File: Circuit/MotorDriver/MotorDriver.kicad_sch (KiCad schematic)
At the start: 21 parts, among them J3 Conn_01x03_Pin, J4 Conn_01x04_Pin, J5 Conn_01x06_Pin, U3 DRV8316RRGFR, U4 XC6206PxxxMR

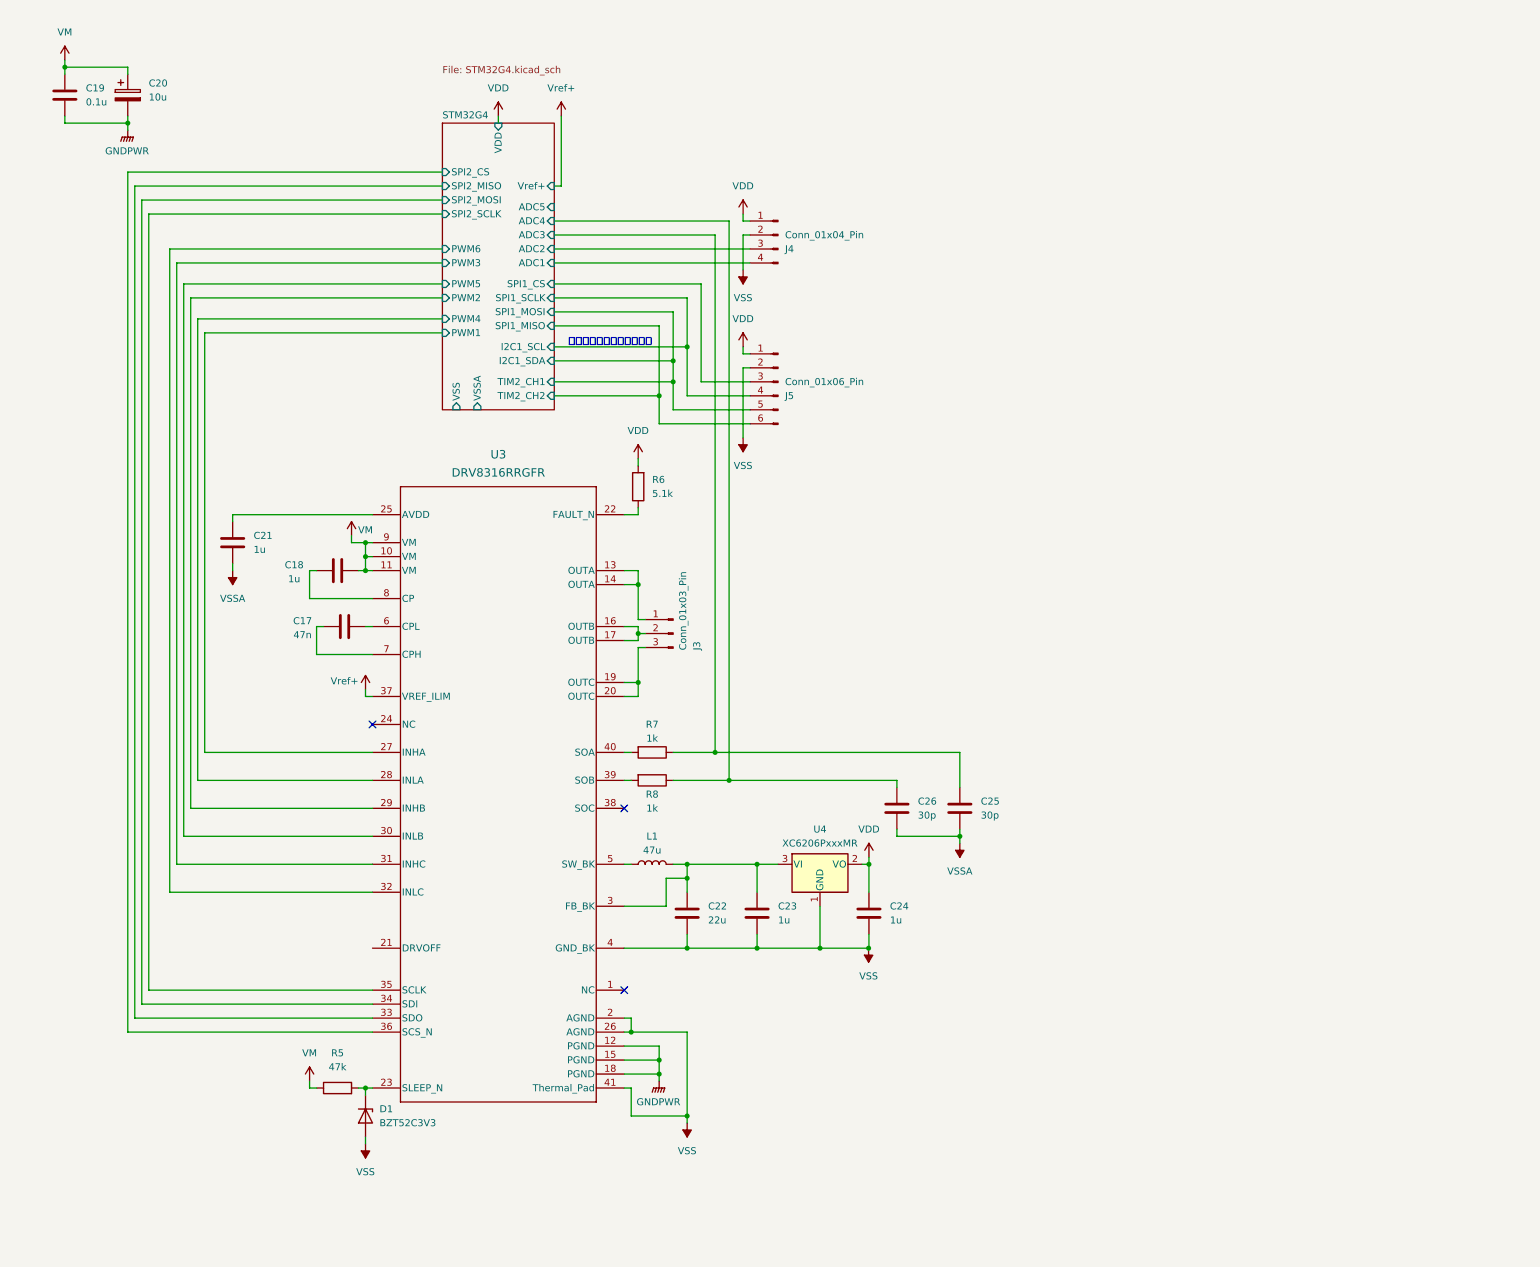
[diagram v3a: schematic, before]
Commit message: GPIOの配線等
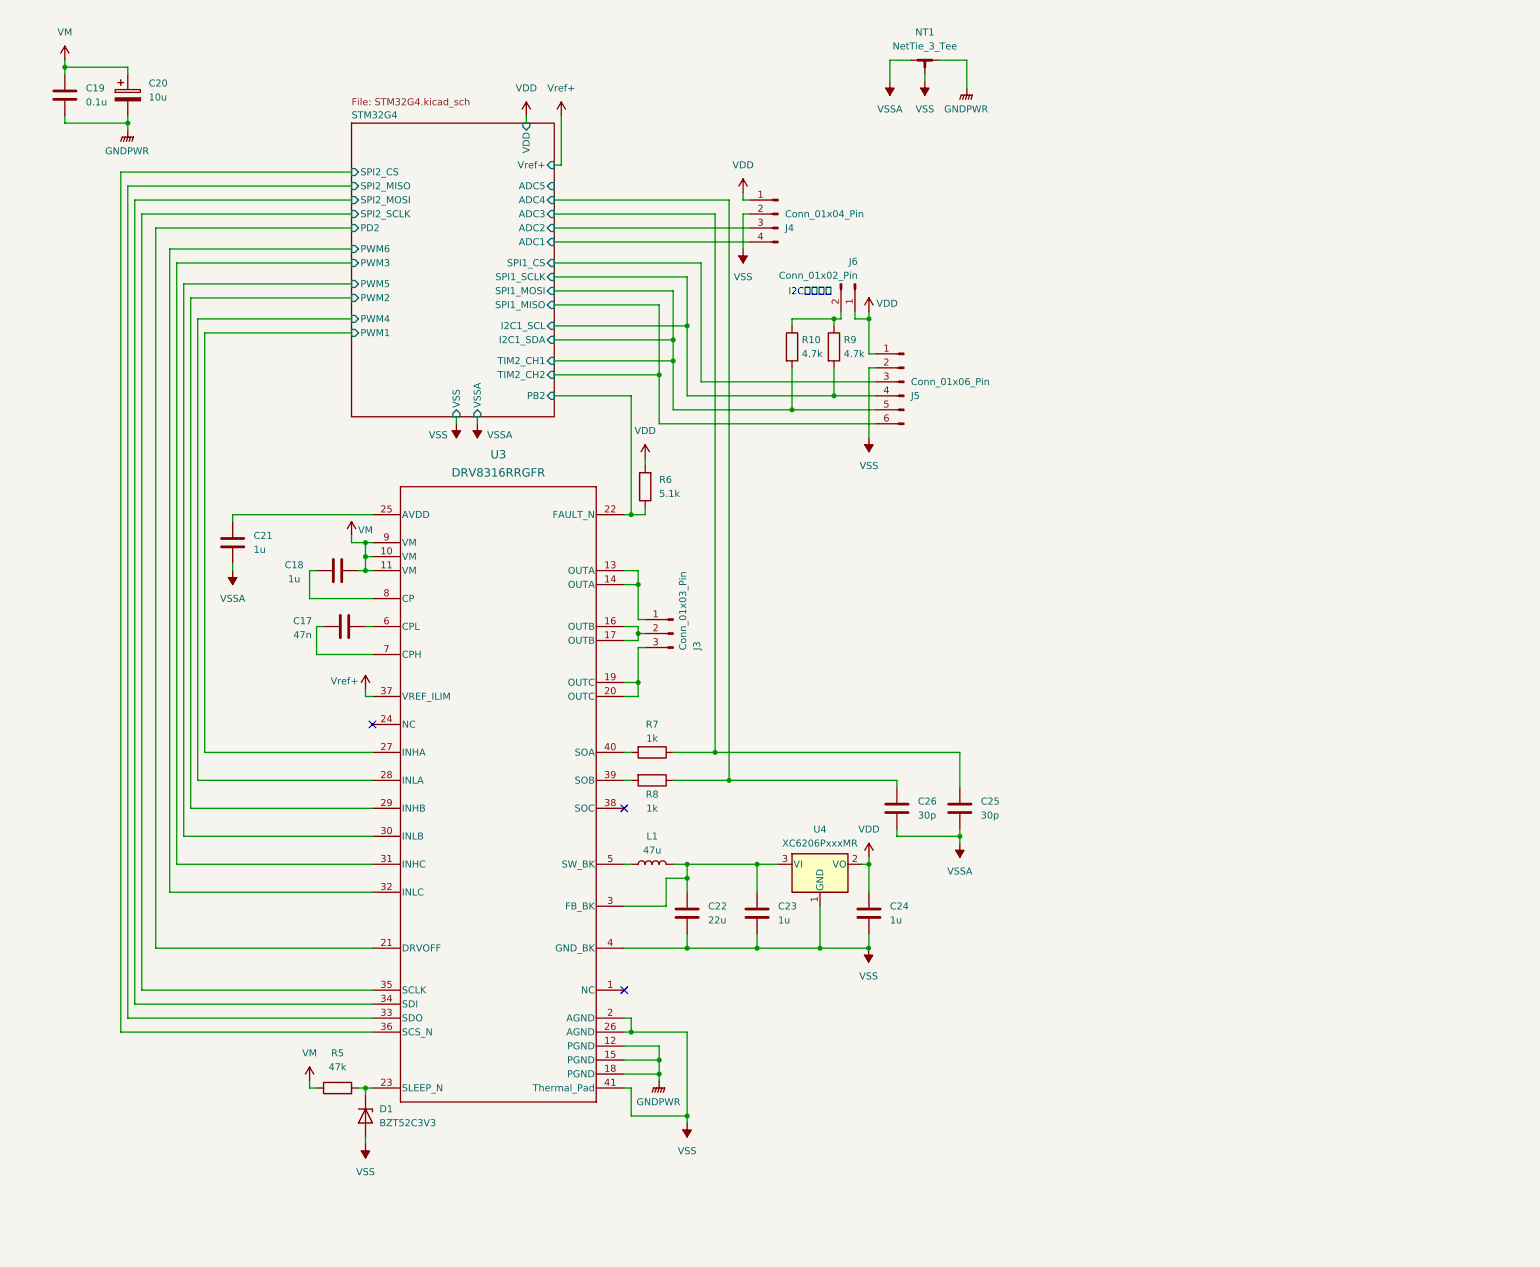
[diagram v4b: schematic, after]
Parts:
- added J6: Conn_01x02_Pin, symbol Connector:Conn_01x02_Pin
- added NT1: NetTie_3_Tee, symbol Device:NetTie_3_Tee
- added R10, R9: 4.7k, symbol Device:R
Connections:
- net GNDPWR: now also NT1.2
- net STM32G4/I2C1_SCL: now also R9.2
- net STM32G4/I2C1_SDA: now also R10.2
- net VDD: now also J6.1 (Pin_1)
- net VSS: now also NT1.3
- net VSSA: now also NT1.1
- net STM32G4/PD2: now reaches U3.21 (DRVOFF)
- net STM32G4/PB2: now reaches R6.1, U3.22 (FAULT_N)
- new net: J6.2 (Pin_2), R10.1, R9.1
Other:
- sheet STM32G4 ports: added PB2, PD2; removed none
- note added: "I2Cの有効化"
- note removed: "プルアップ抵抗どうする？"
- moved on the sheet: J4, J5, R6

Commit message: 回路図完成
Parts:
- added D10: BAT54C, Package_TO_SOT_SMD:SOT-23, symbol Diode:BAT54C
- added D2: LED, symbol Device:LED
- added R11: 4.7k, Resistor_SMD:R_1206_3216Metric, symbol Device:R
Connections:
- net GNDPWR: now also D2.1 (K)
- net VM: now also R11.1
- net at C22.1, L1.2, U3.3 (FB_BK): now also D10.1; no longer C23.1, U4.3 (VI)
- new net: D2.2 (A), R11.2
- new net: C23.1, D10.3, U4.3 (VI)
- new net VBUS: D10.2
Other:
- sheet STM32G4 ports: added VBUS; removed none
- note added: "モータ電源LED(緑)"
- moved on the sheet: C17, C18, C19, C20, C21, C22, C23, C24, C25, C26, D1, J3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

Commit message: JLCPCBの部品は大体フットプリント割り当て完了
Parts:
- C17, C18, C23, C24, C25, C26: footprint (none) -> Capacitor_SMD:C_0603_1608Metric
- C19: footprint (none) -> Capacitor_SMD:C_0402_1005Metric
- C20: footprint (none) -> OU_Capacitor:CP_Radial_D5.0mm_P2.0mm_H11mm_Horizontal1; MPN_URL (none) -> https://akizukidenshi.com/catalog/g/g117901/
- C21: footprint (none) -> Capacitor_SMD:C_0805_2012Metric
- C22: footprint (none) -> Capacitor_SMD:C_1206_3216Metric
- D1: footprint (none) -> Diode_SMD:D_SOD-123
- D2: footprint (none) -> LED_SMD:LED_0805_2012Metric
- L1: footprint (none) -> Inductor_SMD:L_Changjiang_FNR4030S
- R10, R9: footprint (none) -> Resistor_SMD:R_0603_1608Metric
- R5, R6: footprint (none) -> Resistor_SMD:R_0402_1005Metric
- R7, R8: footprint (none) -> Resistor_SMD:R_0805_2012Metric
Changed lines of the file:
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@@
 			)
 		)
-		(property "Footprint" ""
+		(property "Footprint" "Capacitor_SMD:C_1206_3216Metric"
 			(at 135.5852 195.58 0)
 			(hide yes)
@@
 			)
 		)
-		(property "Footprint" ""
+		(property "Footprint" "Capacitor_SMD:C_0603_1608Metric"
 			(at 173.6852 195.58 0)
 			(hide yes)
@@
 			)
 		)
-		(property "Footprint" ""
+		(property "Footprint" "Inductor_SMD:L_Changjiang_FNR4030S"
 			(at 128.27 182.88 0)
 			(hide yes)
@@
 			)
 		)
-		(property "Footprint" ""
+		(property "Footprint" "Resistor_SMD:R_0603_1608Metric"
 			(at 151.892 88.9 90)
 			(hide yes)
@@
 			)
 		)
-		(property "Footprint" ""
+		(property "Footprint" "Capacitor_SMD:C_0402_1005Metric"
 			(at 45.4152 40.64 0)
 			(hide yes)
@@
 			)
 		)
-		(property "Footprint" ""
+		(property "Footprint" "Resistor_SMD:R_0805_2012Metric"
 			(at 128.27 160.782 90)
 			(hide yes)
@@
 			)
 		)
-		(property "Footprint" ""
+		(property "Footprint" "Resistor_SMD:R_0805_2012Metric"
 			(at 128.27 165.862 90)
 			(hide yes)
@@
 			)
 		)
-		(property "Footprint" ""
+		(property "Footprint" "Capacitor_SMD:C_0603_1608Metric"
 			(at 68.58 140.6652 0)
 			(hide yes)
@@
 			)
 		)
-		(property "Footprint" ""
+		(property "Footprint" "Capacitor_SMD:C_0603_1608Metric"
 			(at 188.9252 176.53 0)
 			(hide yes)
@@
 			)
 		)
-		(property "Footprint" ""
+		(property "Footprint" "Diode_SMD:D_SOD-123"
 			(at 76.2 228.6 0)
 			(hide yes)
@@
 			)
 		)
-		(property "Footprint" ""
+		(property "Footprint" "Capacitor_SMD:C_0603_1608Metric"
 			(at 74.93 128.5748 0)
 			(hide yes)
@@
 			)
 		)
-		(property "Footprint" ""
+		(property "Footprint" "Capacitor_SMD:C_0603_1608Metric"
 			(at 147.0152 195.58 0)
 			(hide yes)
@@
 			)
 		)
-		(property "Footprint" ""
+		(property "Footprint" "Capacitor_SMD:C_0603_1608Metric"
 			(at 177.4952 176.53 0)
 			(hide yes)
@@
 			)
 		)
-		(property "Footprint" ""
+		(property "Footprint" "Resistor_SMD:R_0402_1005Metric"
 			(at 71.12 225.298 90)
 			(hide yes)
@@
 			)
 		)
-		(property "Footprint" ""
+		(property "Footprint" "Capacitor_SMD:C_0805_2012Metric"
 			(at 53.0352 128.27 0)
 			(hide yes)
@@
 			)
 		)
-		(property "Footprint" ""
+		(property "Footprint" "Resistor_SMD:R_0603_1608Metric"
 			(at 159.512 88.9 90)
 			(hide yes)
@@
 			)
 		)
-		(property "Footprint" ""
+		(property "Footprint" "LED_SMD:LED_0805_2012Metric"
 			(at 27.94 41.91 0)
 			(hide yes)
@@
 			)
 		)
-		(property "Footprint" ""
+		(property "Footprint" "Resistor_SMD:R_0402_1005Metric"
 			(at 128.778 114.3 90)
 			(hide yes)
@@
 			)
 		)
-		(property "Footprint" ""
+		(property "Footprint" "OU_Capacitor:CP_Radial_D5.0mm_P2.0mm_H11mm_Horizontal1"
 			(at 56.8452 40.64 0)
 			(hide yes)
@@
 			(at 55.88 36.83 0)
 			(hide yes)
+			(show_name no)
+			(do_not_autoplace no)
+			(effects
+				(font
+					(size 1.27 1.27)
+				)
+			)
+		)
+		(property "MPN_URL" "https://akizukidenshi.com/catalog/g/g117901/"
+			(at 55.88 36.83 0)
+			(hide yes)

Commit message: 一部のフットプリントを更新
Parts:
- NT1: footprint (none) -> NetTie:NetTie-3_SMD_Pad2.0mm
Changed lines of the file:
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@@
 			)
 		)
-		(property "Footprint" ""
+		(property "Footprint" "NetTie:NetTie-3_SMD_Pad2.0mm"
 			(at 177.8 36.83 0)
 			(hide yes)
